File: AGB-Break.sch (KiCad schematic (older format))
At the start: 62 parts, among them J1 CONN_WII, J2 Conn_02x03_Odd_Even, J3 Conn_01x02, J4 GameBoy_LinkPort, SW1 SW_Push, U1 AGB-CPU, U2 ATmega328PB-AU, U3 TS5A3160DBV, U4 AGB_SRAM, U5 SpartanEdge, U6 LP5907MFX-2.5, U7 GBA-Slot, U8 Switch-DPDT, Y1 Crystal

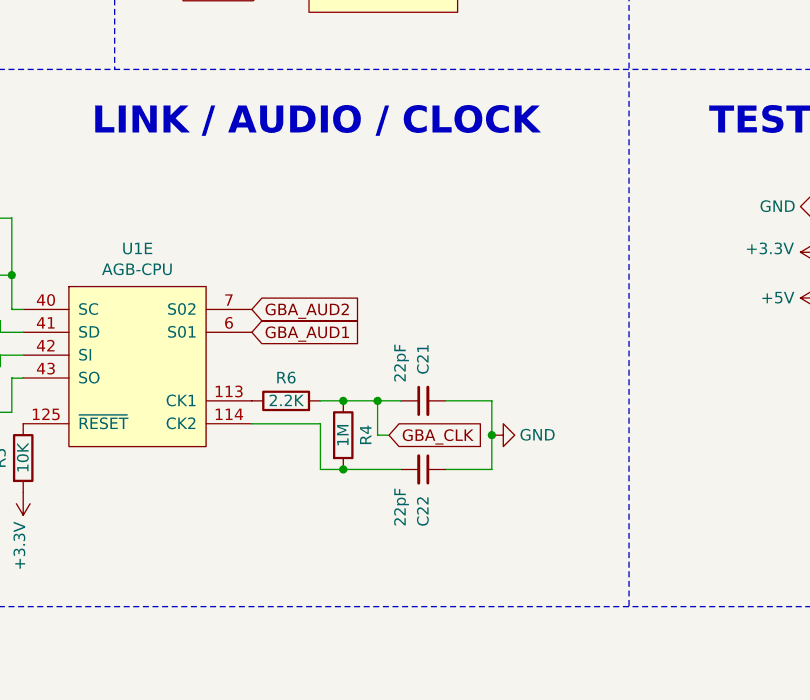
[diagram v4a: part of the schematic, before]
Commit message: Changed clock wiring
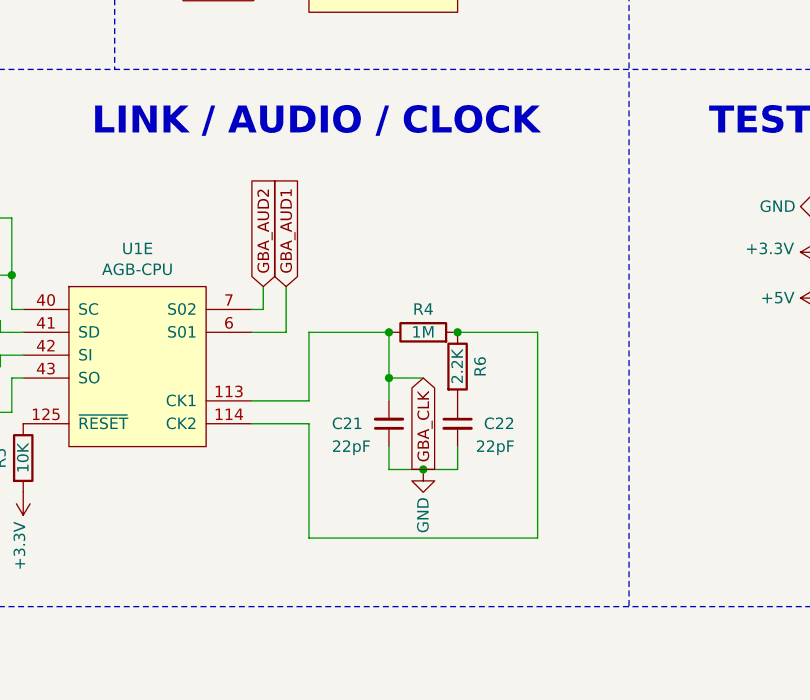
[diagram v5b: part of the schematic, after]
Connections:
- net GBA_CLK: now also C21.2, U1.113 (CK1); no longer C21.1, R6.2
- net GND: now also C21.1, C22.2; no longer C21.2, C22.1
- net at R6.1: now also R4.2, U1.114 (CK2); no longer U1.113 (CK1)
- new net: C22.1, R6.2
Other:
- moved on the sheet: C21, C22, R4, R6
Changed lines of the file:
@@
 	1    0    0    -1
 $EndComp
-Text GLabel 5550 8600 2    50   Input ~ 0
+Text GLabel 5700 8400 1    50   Input ~ 0
 GBA_AUD1
-Text GLabel 5550 8500 2    50   Input ~ 0
+Text GLabel 5600 8400 1    50   Input ~ 0
 GBA_AUD2
 $Comp
@@
 Wire Wire Line
 	11950 2400 11850 2400
-$Comp
-L Device:R R6
-U 1 1 6140FCD0
-P 5700 8900
-F 0 "R6" V 5800 8900 50  0000 C CNN
-F 1 "2.2K" V 5700 8900 50  0000 C CNN
-F 2 "Resistor_SMD:R_0805_2012Metric_Pad1.20x1.40mm_HandSolder" V 5630 8900 50  0001 C CNN
-F 3 "~" H 5700 8900 50  0001 C CNN
-	1    5700 8900
-	0    -1   -1   0
-$EndComp
-$Comp
-L Device:C_Small C21
-U 1 1 614E26BD
-P 6300 8900
-F 0 "C21" H 6550 8900 50  0000 R CNN
-F 1 "22pF" H 6550 9000 50  0000 R CNN
-F 2 "Capacitor_SMD:C_0805_2012Metric_Pad1.18x1.45mm_HandSolder" H 6300 8900 50  0001 C CNN
-F 3 "~" H 6300 8900 50  0001 C CNN
-	1    6300 8900
-	0    -1   -1   0
-$EndComp
-$Comp
-L Device:R R4
-U 1 1 60DB3677
-P 5950 9050
-F 0 "R4" V 6050 9050 50  0000 C CNN
-F 1 "1M" V 5950 9050 50  0000 C CNN
-F 2 "Resistor_SMD:R_0805_2012Metric_Pad1.20x1.40mm_HandSolder" V 5880 9050 50  0001 C CNN
-F 3 "~" H 5950 9050 50  0001 C CNN
-	1    5950 9050
-	1    0    0    -1
-$EndComp
-Text GLabel 6150 9050 2    50   Input ~ 0
-GBA_CLK
-$Comp
-L Device:C_Small C22
-U 1 1 615142E1
-P 6300 9200
-F 0 "C22" H 6550 9200 50  0000 R CNN
-F 1 "22pF" H 6550 9100 50  0000 R CNN
-F 2 "Capacitor_SMD:C_0805_2012Metric_Pad1.18x1.45mm_HandSolder" H 6300 9200 50  0001 C CNN
-F 3 "~" H 6300 9200 50  0001 C CNN
-	1    6300 9200
-	0    1    1    0
-$EndComp
 $Comp
 L power:+3.3V #PWR0132
@@
 Wire Wire Line
 	7050 6200 7050 6250
-Wire Wire Line
-	5850 8900 5950 8900
-Wire Wire Line
-	5550 9000 5850 9000
-Wire Wire Line
-	5850 9000 5850 9200
-Wire Wire Line
-	5850 9200 5950 9200
-Wire Wire Line
-	5950 8900 6100 8900
-Connection ~ 5950 8900
-Wire Wire Line
-	5950 9200 6200 9200
-Connection ~ 5950 9200
-Wire Wire Line
-	6100 8900 6100 9050
-Wire Wire Line
-	6100 9050 6150 9050
-Connection ~ 6100 8900
-Wire Wire Line
-	6100 8900 6200 8900
-Wire Wire Line
-	6400 8900 6600 8900
-Wire Wire Line
-	6600 8900 6600 9050
-Wire Wire Line
-	6600 9200 6400 9200
 NoConn ~ 6650 5600
 NoConn ~ 6650 5700
@@
 NoConn ~ 6650 6100
 NoConn ~ 6650 6300
-$Comp
-L power:GND #PWR0131
-U 1 1 610F66B0
-P 6600 9050
-F 0 "#PWR0131" H 6600 8800 50  0001 C CNN
-F 1 "GND" V 6600 8850 50  0000 C CNN
-F 2 "" H 6600 9050 50  0001 C CNN
-F 3 "" H 6600 9050 50  0001 C CNN
-	1    6600 9050
-	0    -1   -1   0
-$EndComp
-Connection ~ 6600 9050
-Wire Wire Line
-	6600 9050 6600 9200
 $Comp
 L power:GND #PWR0134
@@
 Wire Notes Line
 	1000 9800 9000 9800
+$Comp
+L Device:R R6
+U 1 1 6140FCD0
+P 6450 8750
+F 0 "R6" V 6550 8750 50  0000 C CNN
+F 1 "2.2K" V 6450 8750 50  0000 C CNN
+F 2 "Resistor_SMD:R_0805_2012Metric_Pad1.20x1.40mm_HandSolder" V 6380 8750 50  0001 C CNN
+F 3 "~" H 6450 8750 50  0001 C CNN
+	1    6450 8750
+	1    0    0    -1
+$EndComp
+Wire Wire Line
+	6450 9200 6450 9100
+Wire Wire Line
+	6150 9200 6150 9100
+$Comp
+L Device:C_Small C21
+U 1 1 614E26BD
+P 6150 9000
+F 0 "C21" H 6400 9000 50  0000 R CNN
+F 1 "22pF" H 6400 9100 50  0000 R CNN
+F 2 "Capacitor_SMD:C_0805_2012Metric_Pad1.18x1.45mm_HandSolder" H 6150 9000 50  0001 C CNN
+F 3 "~" H 6150 9000 50  0001 C CNN
+	1    6150 9000
+	-1   0    0    1
+$EndComp
+Text GLabel 6300 8800 3    50   Input ~ 0
+GBA_CLK
+$Comp
+L Device:C_Small C22
+U 1 1 615142E1
+P 6450 9000
+F 0 "C22" H 6700 9000 50  0000 R CNN
+F 1 "22pF" H 6700 8900 50  0000 R CNN
+F 2 "Capacitor_SMD:C_0805_2012Metric_Pad1.18x1.45mm_HandSolder" H 6450 9000 50  0001 C CNN
+F 3 "~" H 6450 9000 50  0001 C CNN
+	1    6450 9000
+	1    0    0    -1
+$EndComp
+Wire Wire Line
+	6450 9200 6300 9200
+$Comp
+L power:GND #PWR0131
+U 1 1 610F66B0
+P 6300 9200
+F 0 "#PWR0131" H 6300 8950 50  0001 C CNN
+F 1 "GND" V 6300 9000 50  0000 C CNN
+F 2 "" H 6300 9200 50  0001 C CNN
+F 3 "" H 6300 9200 50  0001 C CNN
+	1    6300 9200
+	1    0    0    -1
+$EndComp
+Connection ~ 6300 9200
+Wire Wire Line
+	6300 9200 6150 9200
+$Comp
+L Device:R R4
+U 1 1 60DB3677
+P 6300 8600
+F 0 "R4" V 6400 8600 50  0000 C CNN
+F 1 "1M" V 6300 8600 50  0000 C CNN
+F 2 "Resistor_SMD:R_0805_2012Metric_Pad1.20x1.40mm_HandSolder" V 6230 8600 50  0001 C CNN
+F 3 "~" H 6300 8600 50  0001 C CNN
+	1    6300 8600
+	0    -1   -1   0
+$EndComp
+Wire Wire Line
+	6150 8900 6150 8800
+Wire Wire Line
+	6150 8800 6300 8800
+Connection ~ 6150 8800
+Wire Wire Line
+	6150 8600 6150 8800
+Wire Wire Line
+	5550 8500 5600 8500
+Wire Wire Line
+	5600 8500 5600 8400
+Wire Wire Line
+	5550 8600 5700 8600
+Wire Wire Line
+	5700 8600 5700 8400
+Wire Wire Line
+	5550 8900 5800 8900
+Wire Wire Line
+	5800 8900 5800 8600
+Wire Wire Line
+	5800 8600 6150 8600
+Connection ~ 6150 8600
+Wire Wire Line
+	6450 8600 6800 8600
+Wire Wire Line
+	6800 8600 6800 9500
+Wire Wire Line
+	6800 9500 5800 9500
+Wire Wire Line
+	5800 9500 5800 9000
+Wire Wire Line
+	5800 9000 5550 9000
 Wire Bus Line
 	5150 2350 5150 4550
@@
 Wire Bus Line
 	6850 1900 6850 3850
+Connection ~ 6450 8600
 $EndSCHEMATC

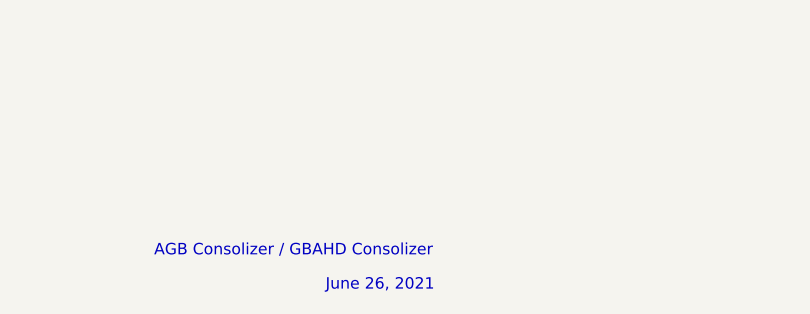
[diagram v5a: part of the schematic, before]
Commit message: Added PDF schematic
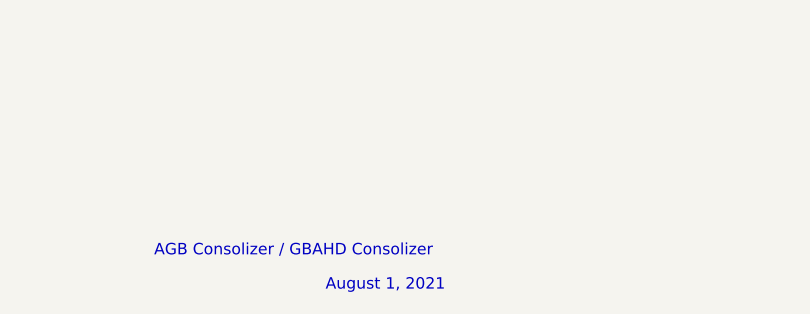
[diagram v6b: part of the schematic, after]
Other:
- note added: "August 1, 2021"
- note removed: "June 26, 2021"
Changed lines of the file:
@@
 AGB Consolizer / GBAHD Consolizer
 Text Notes 13000 11050 0    50   ~ 0
-June 26, 2021
+August 1, 2021
 Text GLabel 5600 5600 0    50   Input ~ 0
 LCD_G5
@@
 Wire Wire Line
 	5800 9000 5550 9000
+Connection ~ 6450 8600
 Wire Bus Line
 	5150 2350 5150 4550
@@
 Wire Bus Line
 	6850 1900 6850 3850
-Connection ~ 6450 8600
 $EndSCHEMATC
